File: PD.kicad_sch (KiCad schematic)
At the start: 66 parts, among them IC1 AOZ2261NQI-11, IC3 AOZ2261NQI-11, IC4 AOZ2261NQI-11, IC5 AOZ2261NQI-11, IC6 AOZ2261NQI-11, IC7 AOZ2261NQI-11

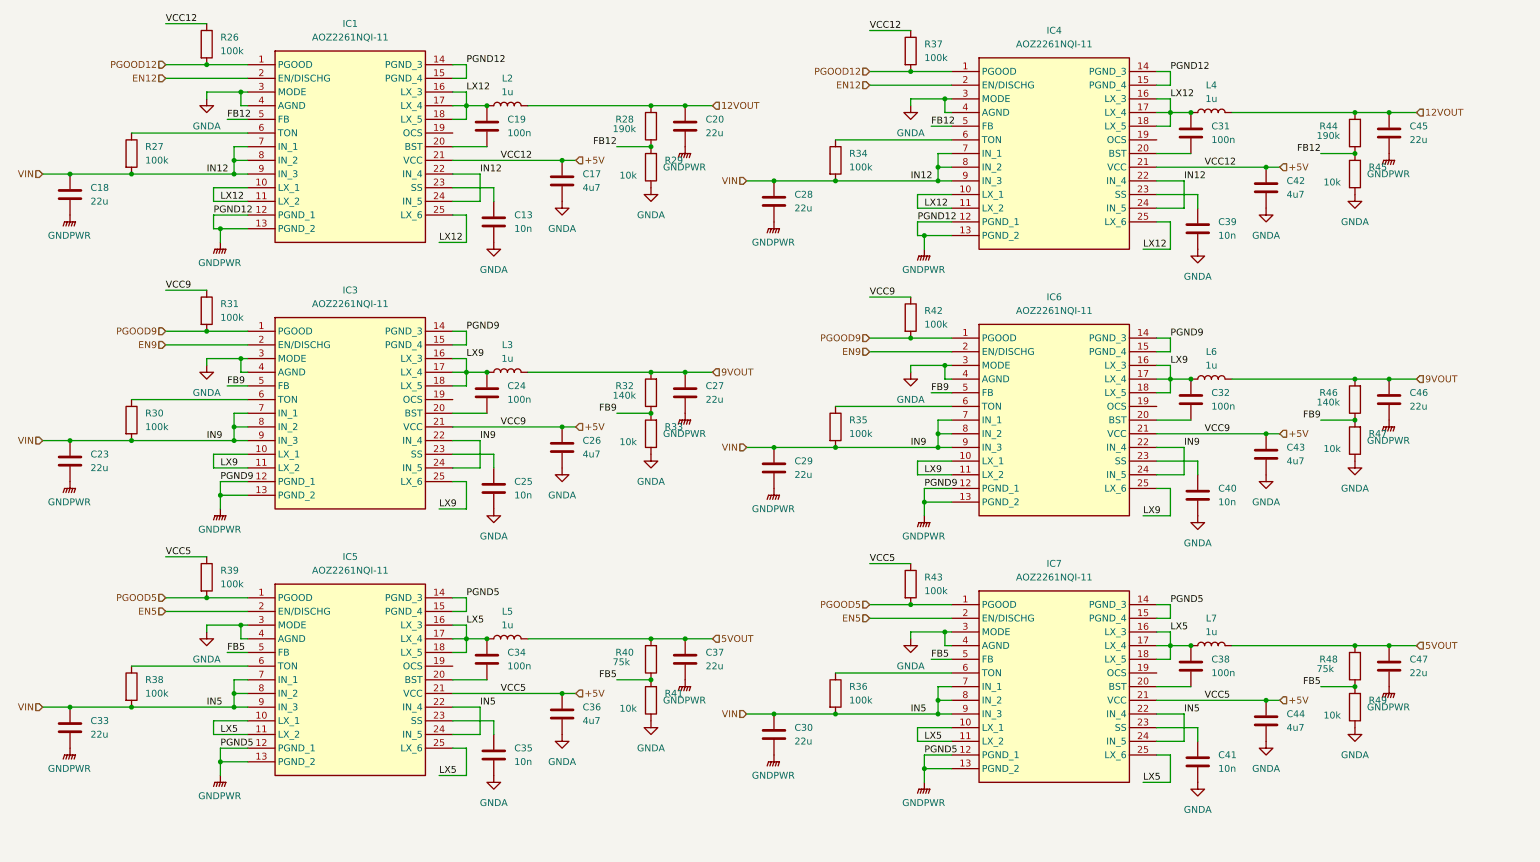
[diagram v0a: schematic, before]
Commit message: Added output and input caps for buck converters into the schematic. Added components into the project specific library.
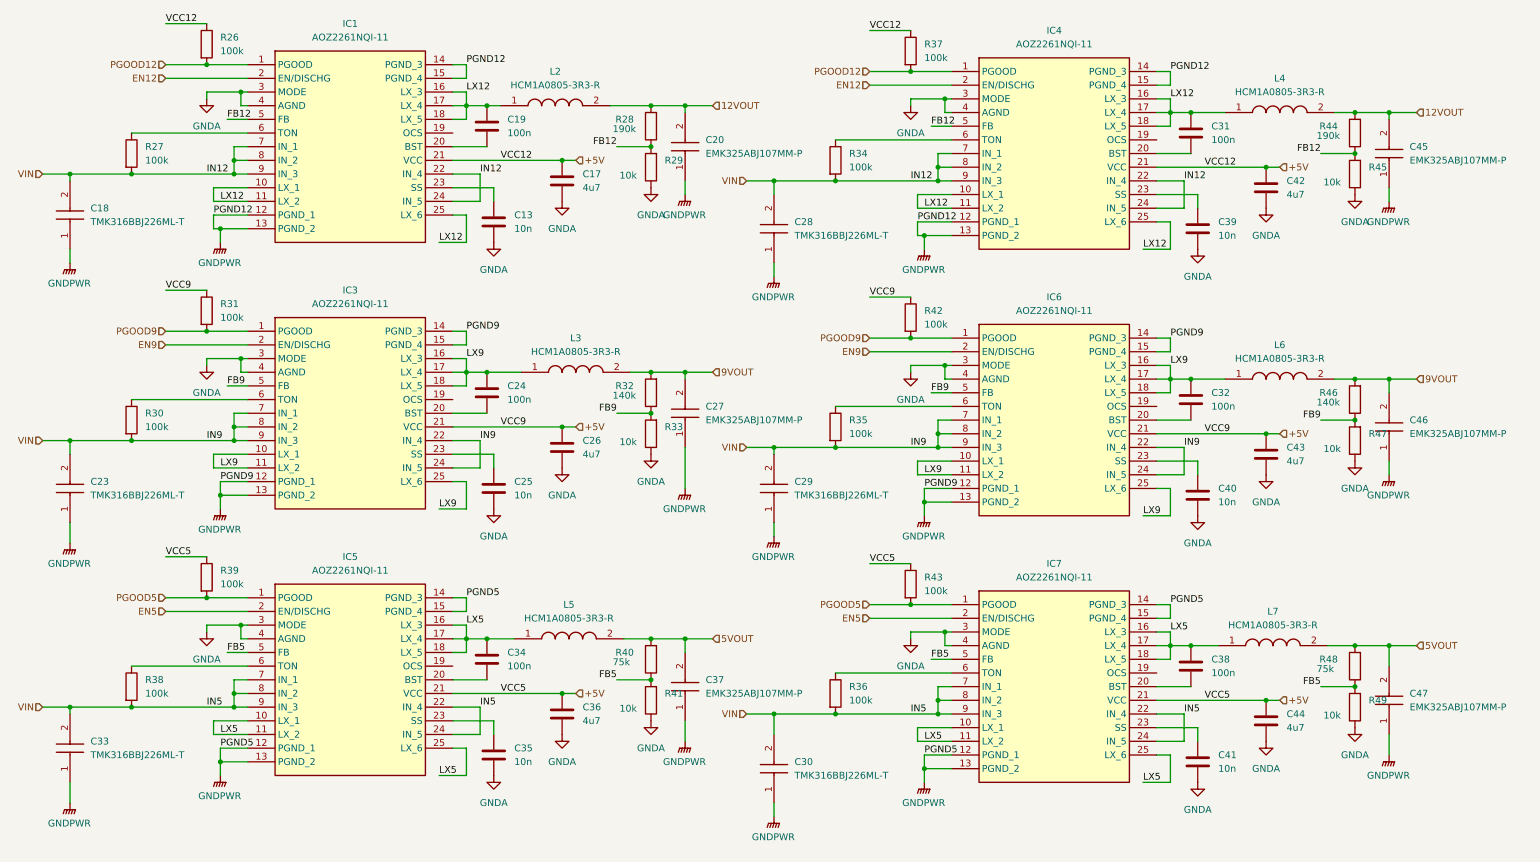
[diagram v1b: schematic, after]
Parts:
- removed C18, C20, C23, C27, C28, C29, C30, C33, C37, C45, C46, C47: 22u, Capacitor_SMD:C_0805_2012Metric_Pad1.18x1.45mm_HandSolder, symbol Device:C
- removed L2, L3, L4, L5, L6, L7: 1u, Inductor_SMD:L_0805_2012Metric_Pad1.15x1.40mm_HandSolder, symbol Device:L
- added C18, C23, C28, C29, C30, C33: TMK316BBJ226ML-T, CAPC3216X190N, symbol TMK316BBJ226ML-T:TMK316BBJ226ML-T
- added C20, C27, C37, C45, C46, C47: EMK325ABJ107MM-P, CAPC3225X270N, symbol EMK325ABJ107MM-P:EMK325ABJ107MM-P
- added L2, L3, L4, L5, L6, L7: HCM1A0805-3R3-R, INDPM8180X540N, symbol HCM1A0805-3R3-R:HCM1A0805-3R3-R
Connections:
- net 12VOUT: now also C20.2, C45.2, L2.2, L4.2
- net 5VOUT: now also C37.2, C47.2, L5.2, L7.2
- net 9VOUT: now also C27.2, C46.2, L3.2, L6.2
- net GNDPWR: now also C18.1, C20.1, C23.1, C27.1, C28.1, C29.1, C30.1, C33.1, C37.1, C45.1, C46.1, C47.1
- net LX12: now also L2.1, L4.1
- net LX5: now also L5.1, L7.1
- net LX9: now also L3.1, L6.1
- net VIN: now also C18.2, C23.2, C28.2, C29.2, C30.2, C33.2

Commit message: Changed RTon values to get reasonable osscilation frequencies for all the buck converters, added 10K current limit resistors to all the OCS pins, adjusted some net names to be different for the two buck converters at each voltage
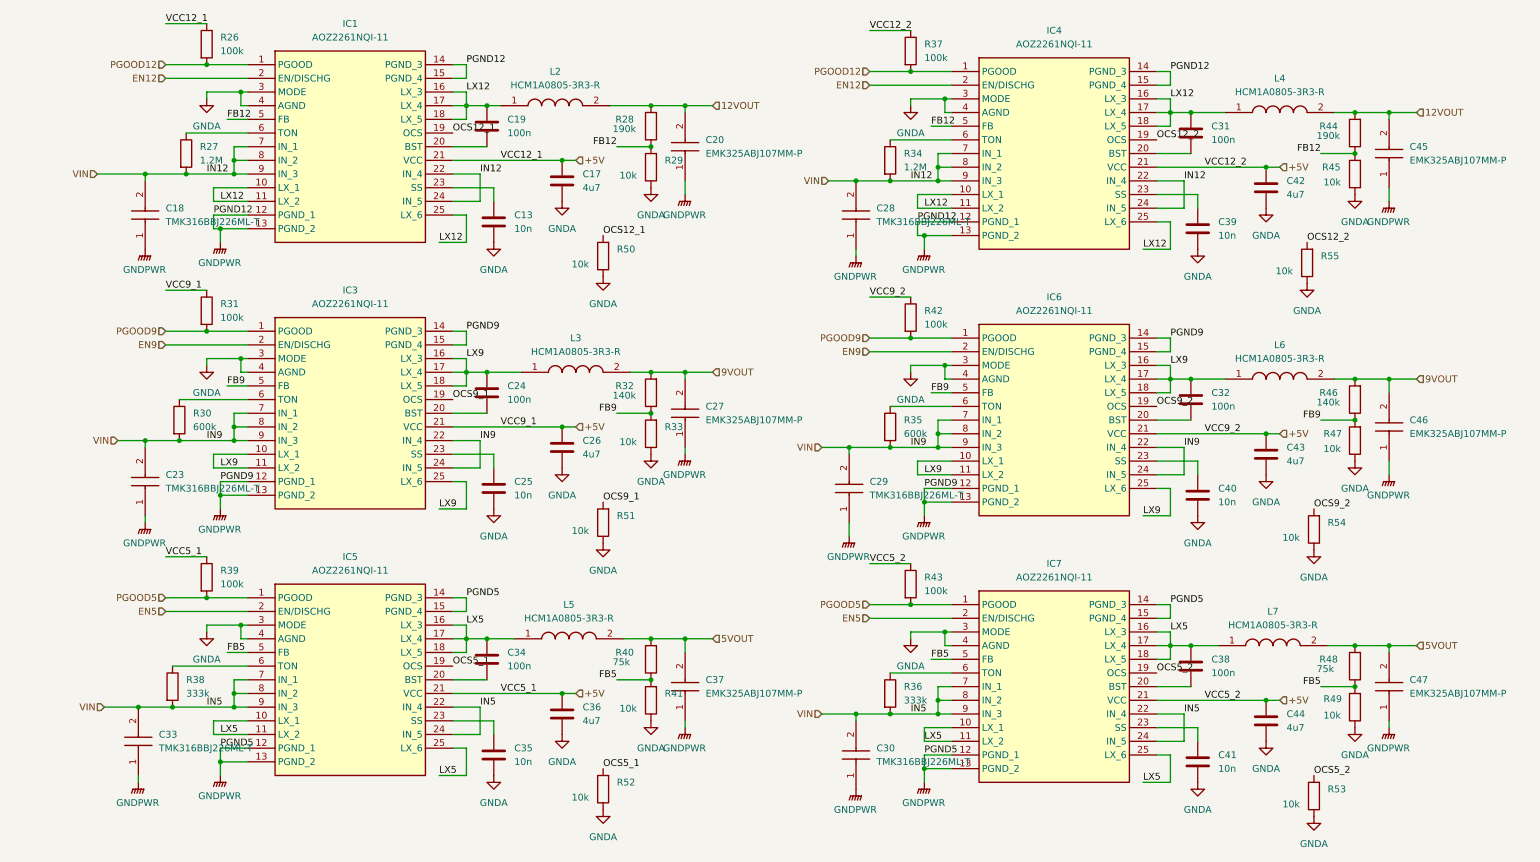
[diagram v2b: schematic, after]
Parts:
- added R50, R51, R52, R53, R54, R55: 10k, Resistor_SMD:R_0805_2012Metric_Pad1.20x1.40mm_HandSolder, symbol Device:R
- R27, R34: value 100k -> 1.2M
- R30, R35: value 100k -> 600k
- R36, R38: value 100k -> 333k
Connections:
- net GNDA: now also R50.1, R51.1, R52.1, R53.1, R54.1, R55.1
- net OCS12_1: now reaches IC1.19 (OCS)
- net OCS12_1: now also R50.2
- net OCS5_1: now reaches IC5.19 (OCS)
- net OCS5_1: now also R52.2
- net OCS5_2: now reaches IC7.19 (OCS)
- net OCS5_2: now also R53.2
- net OCS9_2: now reaches IC6.19 (OCS)
- net OCS9_2: now also R54.2
- net OCS9_1: now reaches IC3.19 (OCS)
- net OCS9_1: now also R51.2
- net OCS12_2: now reaches IC4.19 (OCS)
- net OCS12_2: now also R55.2
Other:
- moved on the sheet: C18, C23, C28, C29, C30, C33, C47, R27, R30, R34, R35, R36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

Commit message: Added A and Bonto the all the net labels and sheet outputs for the pairs of buck converters. Moved the XT90 connector for the battery input to the connectors sectionof the main sheet and renamed the nodes to BAT+ and BAT-. Added some comments clarifying the purpose of some connectors and which grounds go to which device.
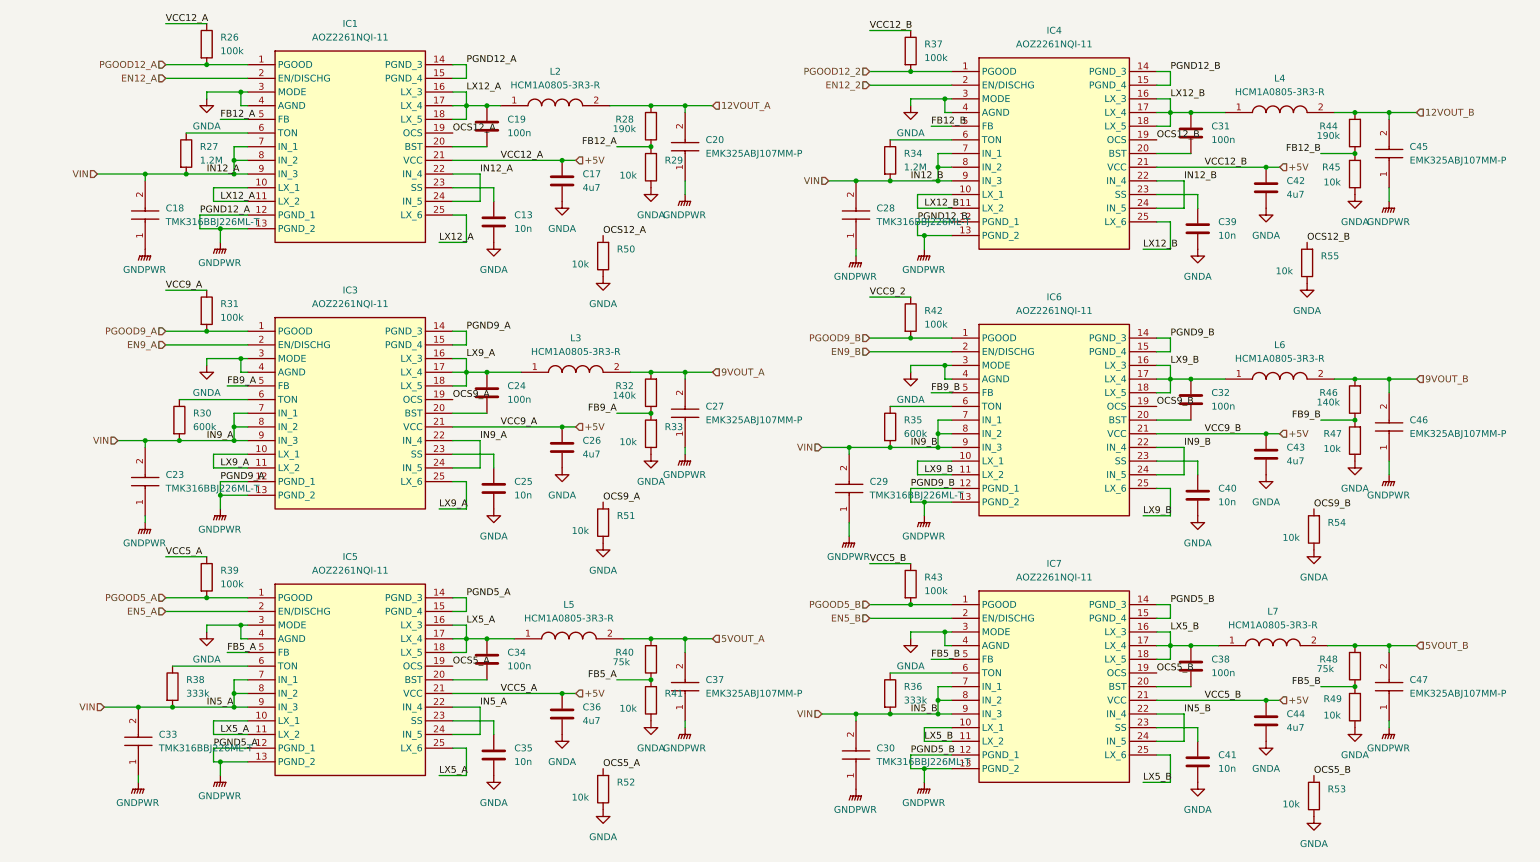
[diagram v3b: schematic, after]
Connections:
- net +5V: no longer R42.1
- net 12VOUT renamed 12VOUT_A
- net 12VOUT_A: no longer C45.2, L4.2, R44.2
- net 5VOUT renamed 5VOUT_A
- net 5VOUT_A: no longer C47.2, L7.2, R48.2
- net 9VOUT renamed 9VOUT_A
- net 9VOUT_A: no longer C46.2, L6.2, R46.2
- net EN12 renamed EN12_2
- net EN12_2: no longer IC1.2 (EN/DISCHG)
- net EN5 renamed EN5_A
- net EN5_A: no longer IC7.2 (EN/DISCHG)
- net EN9 renamed EN9_A
- net EN9_A: no longer IC6.2 (EN/DISCHG)
- net FB12 renamed FB12_A
- net FB12_A: no longer IC4.5 (FB), R44.1, R45.2
- net FB5 renamed FB5_A
- net FB5_A: no longer IC7.5 (FB), R48.1, R49.2
- net FB9 renamed FB9_A
- net FB9_A: no longer IC6.5 (FB), R46.1, R47.2
- net LX12 renamed LX12_A
- net LX12_A: no longer C31.1, IC4.10 (LX_1), IC4.11 (LX_2), IC4.16 (LX_3), IC4.17 (LX_4), IC4.18 (LX_5), IC4.25 (LX_6), L4.1
- net LX5 renamed LX5_A
- net LX5_A: no longer C38.1, IC7.10 (LX_1), IC7.11 (LX_2), IC7.16 (LX_3), IC7.17 (LX_4), IC7.18 (LX_5), IC7.25 (LX_6), L7.1
- net LX9 renamed LX9_A
- net LX9_A: no longer C32.1, IC6.10 (LX_1), IC6.11 (LX_2), IC6.16 (LX_3), IC6.17 (LX_4), IC6.18 (LX_5), IC6.25 (LX_6), L6.1
- net OCS12_1 renamed OCS12_A
- net OCS12_2 renamed OCS12_B
- net OCS5_1 renamed OCS5_A
- net OCS5_2 renamed OCS5_B
- net OCS9_1 renamed OCS9_A
- net OCS9_2 renamed OCS9_B
- net PGOOD12 renamed PGOOD12_2
- net PGOOD12_2: no longer IC1.1 (PGOOD), R26.2
- net PGOOD5 renamed PGOOD5_A
- net PGOOD5_A: no longer IC7.1 (PGOOD), R43.2
- net PGOOD9  renamed PGOOD9_A
- net PGOOD9_A: no longer IC6.1 (PGOOD), R42.2
- new net 12VOUT_B: C45.2, L4.2, R44.2
- new net 5VOUT_B: C47.2, L7.2, R48.2
- new net 9VOUT_B: C46.2, L6.2, R46.2
- new net EN12_A: IC1.2 (EN/DISCHG)
- new net EN5_B: IC7.2 (EN/DISCHG)
- new net EN9_B: IC6.2 (EN/DISCHG)
- new net FB12_B: IC4.5 (FB), R44.1, R45.2
- new net FB5_B: IC7.5 (FB), R48.1, R49.2
- new net FB9_B: IC6.5 (FB), R46.1, R47.2
- new net LX12_B: C31.1, IC4.10 (LX_1), IC4.11 (LX_2), IC4.16 (LX_3), IC4.17 (LX_4), IC4.18 (LX_5), IC4.25 (LX_6), L4.1
- new net LX5_B: C38.1, IC7.10 (LX_1), IC7.11 (LX_2), IC7.16 (LX_3), IC7.17 (LX_4), IC7.18 (LX_5), IC7.25 (LX_6), L7.1
- new net LX9_B: C32.1, IC6.10 (LX_1), IC6.11 (LX_2), IC6.16 (LX_3), IC6.17 (LX_4), IC6.18 (LX_5), IC6.25 (LX_6), L6.1
- new net PGOOD12_A: IC1.1 (PGOOD), R26.2
- new net PGOOD5_B: IC7.1 (PGOOD), R43.2
- new net PGOOD9_B: IC6.1 (PGOOD), R42.2
- new net VCC9_2: R42.1
